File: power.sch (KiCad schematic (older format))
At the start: 50 parts, among them CN8 Power_Conn, U1 68000D, U10 74LS244, U11 74LS373, U12 74LS244, U13 74LS373, U2 FAT_AGNUS_8375, U32 74LS139, U34 74LS373, U35 74LS244, U36 74LS05, U37 74LS32, U5 GARY_5719, X1 XTAL

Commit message: Top layer done!
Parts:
- X1: footprint Oscillator:Oscillator_SMD_TXC_7C-4Pin_5.0x3.2mm -> Raemixx500:Xtal
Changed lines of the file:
@@
 F 0 "X1" H 5970 5260 50  0000 L CNN
 F 1 "XTAL" H 6020 4660 50  0000 L CNN
-F 2 "Oscillator:Oscillator_SMD_TXC_7C-4Pin_5.0x3.2mm" H 5970 4360 50  0001 C CNN
+F 2 "Raemixx500:Xtal" H 5970 4360 50  0001 C CNN
 F 3 "http://www.txccorp.com/download/products/osc/7C_o.pdf" H 5770 5010 50  0001 C CNN
 	2    5870 5010

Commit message: Wire Power Connector (Original+DIN-5)
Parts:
- CN8: footprint w_conn_av:din-5 -> Raemixx500:power_ami+din5
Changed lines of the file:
@@
 F 0 "CN8" H 2930 2180 50  0000 C CNN
 F 1 "Power_Conn" H 2680 2280 50  0001 C CNN
-F 2 "w_conn_av:din-5" H 870 2390 50  0001 C CNN
+F 2 "Raemixx500:power_ami+din5" H 870 2390 50  0001 C CNN
 F 3 "~" H 870 2390 50  0001 C CNN
 	1    2820 1940

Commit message: Fix power connector label
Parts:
- CN8: value Power_Conn -> POWER
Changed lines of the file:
@@
 P 2820 1940
 F 0 "CN8" H 2930 2180 50  0000 C CNN
-F 1 "Power_Conn" H 2680 2280 50  0001 C CNN
+F 1 "POWER" H 2680 2280 50  0001 C CNN
 F 2 "Raemixx500:power_ami+din5" H 870 2390 50  0001 C CNN
 F 3 "~" H 870 2390 50  0001 C CNN

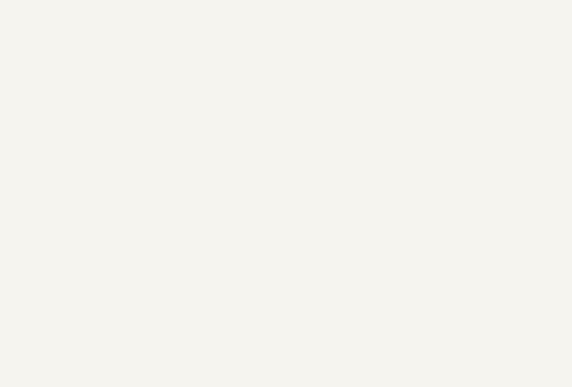
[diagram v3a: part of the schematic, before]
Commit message: Fix a lot of ERC/DRC errors
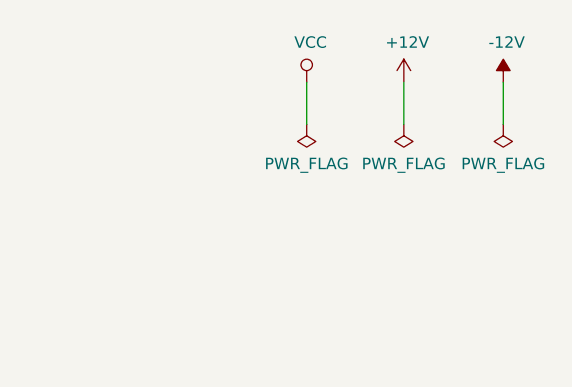
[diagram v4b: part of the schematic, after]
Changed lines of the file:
@@
 EESchema Schematic File Version 4
-LIBS:Raemix500-cache
-EELAYER 29 0
+EELAYER 30 0
 EELAYER END
 $Descr A3 16535 11693
@@
 Sheet 12 14
 Title "Rämixx500"
-Date "2019-04-20"
+Date "2020-04-04"
 Rev "1git"
 Comp "SukkoPera"
@@
 	3415 1770 3540 1770
 Connection ~ 3270 1670
+$Comp
+L power:+12V #PWR?
+U 1 1 5F4FF100
+P 15300 810
+AR Path="/5D2DC3A1/5F4FF100" Ref="#PWR?"  Part="1"
+AR Path="/5E9E4C57/5F4FF100" Ref="#PWR0271"  Part="1"
+F 0 "#PWR0271" H 15300 660 50  0001 C CNN
+F 1 "+12V" H 15315 983 50  0000 C CNN
+F 2 "" H 15300 810 50  0001 C CNN
+F 3 "" H 15300 810 50  0001 C CNN
+	1    15300 810
+	1    0    0    -1
+$EndComp
+$Comp
+L power:-12V #PWR?
+U 1 1 5F500001
+P 15735 810
+AR Path="/5D2DC3A1/5F500001" Ref="#PWR?"  Part="1"
+AR Path="/5E9E4C57/5F500001" Ref="#PWR0272"  Part="1"
+F 0 "#PWR0272" H 15735 910 50  0001 C CNN
+F 1 "-12V" H 15750 983 50  0000 C CNN
+F 2 "" H 15735 810 50  0001 C CNN
+F 3 "" H 15735 810 50  0001 C CNN
+	1    15735 810
+	1    0    0    -1
+$EndComp
+$Comp
+L power:VCC #PWR0273
+U 1 1 5F50042E
+P 14875 810
+F 0 "#PWR0273" H 14875 660 50  0001 C CNN
+F 1 "VCC" H 14892 983 50  0000 C CNN
+F 2 "" H 14875 810 50  0001 C CNN
+F 3 "" H 14875 810 50  0001 C CNN
+	1    14875 810
+	1    0    0    -1
+$EndComp
+$Comp
+L power:PWR_FLAG #FLG0106
+U 1 1 5F500F21
+P 14875 995
+F 0 "#FLG0106" H 14875 1070 50  0001 C CNN
+F 1 "PWR_FLAG" H 14875 1168 50  0000 C CNN
+F 2 "" H 14875 995 50  0001 C CNN
+F 3 "~" H 14875 995 50  0001 C CNN
+	1    14875 995
+	-1   0    0    1
+$EndComp
+Wire Wire Line
+	14875 995  14875 810
+$Comp
+L power:PWR_FLAG #FLG0107
+U 1 1 5F50D532
+P 15300 995
+F 0 "#FLG0107" H 15300 1070 50  0001 C CNN
+F 1 "PWR_FLAG" H 15300 1168 50  0000 C CNN
+F 2 "" H 15300 995 50  0001 C CNN
+F 3 "~" H 15300 995 50  0001 C CNN
+	1    15300 995
+	-1   0    0    1
+$EndComp
+Wire Wire Line
+	15300 995  15300 810
+$Comp
+L power:PWR_FLAG #FLG0108
+U 1 1 5F519A88
+P 15735 995
+F 0 "#FLG0108" H 15735 1070 50  0001 C CNN
+F 1 "PWR_FLAG" H 15735 1168 50  0000 C CNN
+F 2 "" H 15735 995 50  0001 C CNN
+F 3 "~" H 15735 995 50  0001 C CNN
+	1    15735 995
+	-1   0    0    1
+$EndComp
+Wire Wire Line
+	15735 995  15735 810
 $EndSCHEMATC

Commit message: Use KiCad footprint for oscillator
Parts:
- X1: footprint Raemixx500:Xtal -> Oscillator:Oscillator_DIP-14
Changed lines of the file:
@@
 F 0 "X1" H 5970 5260 50  0000 L CNN
 F 1 "XTAL" H 6020 4660 50  0000 L CNN
-F 2 "Raemixx500:Xtal" H 5970 4360 50  0001 C CNN
+F 2 "Oscillator:Oscillator_DIP-14" H 5970 4360 50  0001 C CNN
 F 3 "http://www.txccorp.com/download/products/osc/7C_o.pdf" H 5770 5010 50  0001 C CNN
 	2    5870 5010
